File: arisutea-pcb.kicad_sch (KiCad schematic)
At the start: 41 parts, among them U1 USBLC6-2SC6, U2 ATMEGA32U4_QFN44, Y1 16MHz_Crystal_GND24

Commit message: added MOAR LEDZZZZZZZZZ
5 more to be exact.
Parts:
- LOGO3, LOGO4: value QMK Logo -> mattyams logo; footprint arisutea:OSHW-Logo_11.4x12mm_SilkScreen -> 3x6_graphics:mattyams_logo

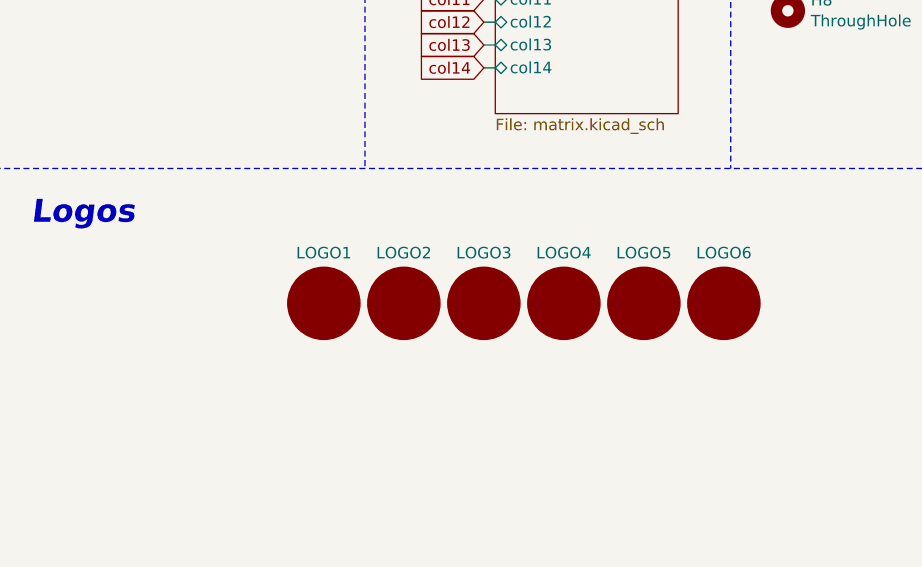
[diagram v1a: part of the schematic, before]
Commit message: added different logo, redid gerbies
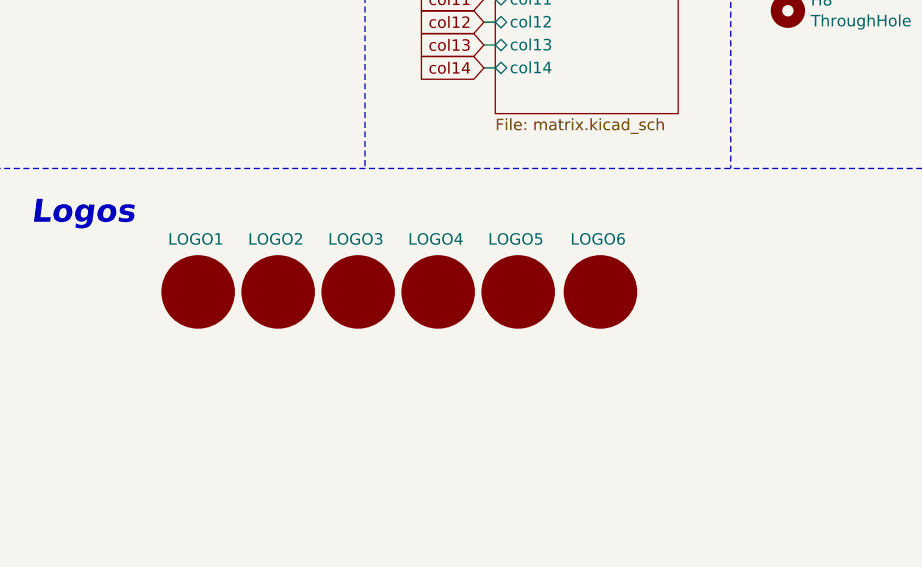
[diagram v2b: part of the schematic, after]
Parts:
- LOGO3, LOGO4: value mattyams logo -> OSHW Logo; footprint 3x6_graphics:mattyams_logo -> arisutea:OSHW-Logo_11.4x12mm_SilkScreen
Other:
- moved on the sheet: LOGO1, LOGO2, LOGO3, LOGO4, LOGO5, LOGO6
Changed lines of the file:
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@@
     (pin "C")
   )
-  (symbol (lib_id "arisutea-pcb:LOGO") (at 213.614 158.242 0) (unit 1)
-    (in_bom yes) (on_board yes)
-    (property "Reference" "LOGO1" (id 0) (at 213.614 152.654 0))
-    (property "Value" "arisutea_logo" (id 1) (at 215.519 148.7424 0)
-      (effects (font (size 1.27 1.27)) hide)
-    )
-    (property "Footprint" "arisutea:arisutea_logo" (id 2) (at 213.614 149.352 0)
-      (effects (font (size 1.27 1.27)) hide)
-    )
-    (property "Datasheet" "" (id 3) (at 213.614 149.352 0)
-      (effects (font (size 1.27 1.27)) hide)
-    )
-  )
-  (symbol (lib_id "arisutea-pcb:LOGO") (at 222.504 158.242 0) (unit 1)
-    (in_bom yes) (on_board yes)
-    (property "Reference" "LOGO2" (id 0) (at 222.504 152.654 0))
-    (property "Value" "arisutea_logo" (id 1) (at 224.409 148.7424 0)
-      (effects (font (size 1.27 1.27)) hide)
-    )
-    (property "Footprint" "arisutea:arisutea_logo" (id 2) (at 222.504 149.352 0)
-      (effects (font (size 1.27 1.27)) hide)
-    )
-    (property "Datasheet" "" (id 3) (at 222.504 149.352 0)
-      (effects (font (size 1.27 1.27)) hide)
-    )
-  )
-  (symbol (lib_id "arisutea-pcb:LOGO") (at 231.394 158.242 0) (unit 1)
-    (in_bom yes) (on_board yes)
-    (property "Reference" "LOGO3" (id 0) (at 231.394 152.654 0))
-    (property "Value" "mattyams logo" (id 1) (at 233.299 148.7424 0)
-      (effects (font (size 1.27 1.27)) hide)
-    )
-    (property "Footprint" "3x6_graphics:mattyams_logo" (id 2) (at 231.394 149.352 0)
-      (effects (font (size 1.27 1.27)) hide)
-    )
-    (property "Datasheet" "" (id 3) (at 231.394 149.352 0)
-      (effects (font (size 1.27 1.27)) hide)
-    )
-  )
-  (symbol (lib_id "arisutea-pcb:LOGO") (at 240.284 158.242 0) (unit 1)
-    (in_bom yes) (on_board yes)
-    (property "Reference" "LOGO4" (id 0) (at 240.284 152.654 0))
-    (property "Value" "mattyams logo" (id 1) (at 242.189 148.7424 0)
-      (effects (font (size 1.27 1.27)) hide)
-    )
-    (property "Footprint" "3x6_graphics:mattyams_logo" (id 2) (at 240.284 149.352 0)
-      (effects (font (size 1.27 1.27)) hide)
-    )
-    (property "Datasheet" "" (id 3) (at 240.284 149.352 0)
-      (effects (font (size 1.27 1.27)) hide)
-    )
-  )
-  (symbol (lib_id "arisutea-pcb:LOGO") (at 249.174 158.242 0) (unit 1)
-    (in_bom yes) (on_board yes)
-    (property "Reference" "LOGO5" (id 0) (at 249.174 152.654 0))
-    (property "Value" "QMK_Logo_Light" (id 1) (at 251.079 148.7424 0)
-      (effects (font (size 1.27 1.27)) hide)
-    )
-    (property "Footprint" "arisutea:QMK_Logo_Light" (id 2) (at 249.174 149.352 0)
-      (effects (font (size 1.27 1.27)) hide)
-    )
-    (property "Datasheet" "" (id 3) (at 249.174 149.352 0)
-      (effects (font (size 1.27 1.27)) hide)
-    )
-  )
-  (symbol (lib_id "arisutea-pcb:LOGO") (at 258.064 158.242 0) (unit 1)
-    (in_bom yes) (on_board yes)
-    (property "Reference" "LOGO6" (id 0) (at 258.064 152.654 0))
-    (property "Value" "QMK_Logo_Light" (id 1) (at 259.969 148.7424 0)
-      (effects (font (size 1.27 1.27)) hide)
-    )
-    (property "Footprint" "arisutea:QMK_Logo_Light" (id 2) (at 258.064 149.352 0)
-      (effects (font (size 1.27 1.27)) hide)
-    )
-    (property "Datasheet" "" (id 3) (at 258.064 149.352 0)
+  (symbol (lib_id "arisutea-pcb:LOGO") (at 199.644 156.972 0) (unit 1)
+    (in_bom yes) (on_board yes)
+    (property "Reference" "LOGO1" (id 0) (at 199.39 151.13 0))
+    (property "Value" "arisutea_logo" (id 1) (at 201.549 147.4724 0)
+      (effects (font (size 1.27 1.27)) hide)
+    )
+    (property "Footprint" "arisutea:arisutea_logo" (id 2) (at 199.644 148.082 0)
+      (effects (font (size 1.27 1.27)) hide)
+    )
+    (property "Datasheet" "" (id 3) (at 199.644 148.082 0)
+      (effects (font (size 1.27 1.27)) hide)
+    )
+  )
+  (symbol (lib_id "arisutea-pcb:LOGO") (at 208.534 156.972 0) (unit 1)
+    (in_bom yes) (on_board yes)
+    (property "Reference" "LOGO2" (id 0) (at 208.28 151.13 0))
+    (property "Value" "arisutea_logo" (id 1) (at 210.439 147.4724 0)
+      (effects (font (size 1.27 1.27)) hide)
+    )
+    (property "Footprint" "arisutea:arisutea_logo" (id 2) (at 208.534 148.082 0)
+      (effects (font (size 1.27 1.27)) hide)
+    )
+    (property "Datasheet" "" (id 3) (at 208.534 148.082 0)
+      (effects (font (size 1.27 1.27)) hide)
+    )
+  )
+  (symbol (lib_id "arisutea-pcb:LOGO") (at 217.424 156.972 0) (unit 1)
+    (in_bom yes) (on_board yes)
+    (property "Reference" "LOGO3" (id 0) (at 217.17 151.13 0))
+    (property "Value" "OSHW Logo" (id 1) (at 219.329 147.4724 0)
+      (effects (font (size 1.27 1.27)) hide)
+    )
+    (property "Footprint" "arisutea:OSHW-Logo_11.4x12mm_SilkScreen" (id 2) (at 217.424 148.082 0)
+      (effects (font (size 1.27 1.27)) hide)
+    )
+    (property "Datasheet" "" (id 3) (at 217.424 148.082 0)
+      (effects (font (size 1.27 1.27)) hide)
+    )
+  )
+  (symbol (lib_id "arisutea-pcb:LOGO") (at 226.314 156.972 0) (unit 1)
+    (in_bom yes) (on_board yes)
+    (property "Reference" "LOGO4" (id 0) (at 226.06 151.13 0))
+    (property "Value" "OSHW Logo" (id 1) (at 228.219 147.4724 0)
+      (effects (font (size 1.27 1.27)) hide)
+    )
+    (property "Footprint" "arisutea:OSHW-Logo_11.4x12mm_SilkScreen" (id 2) (at 226.314 148.082 0)
+      (effects (font (size 1.27 1.27)) hide)
+    )
+    (property "Datasheet" "" (id 3) (at 226.314 148.082 0)
+      (effects (font (size 1.27 1.27)) hide)
+    )
+  )
+  (symbol (lib_id "arisutea-pcb:LOGO") (at 235.204 156.972 0) (unit 1)
+    (in_bom yes) (on_board yes)
+    (property "Reference" "LOGO5" (id 0) (at 234.95 151.13 0))
+    (property "Value" "QMK_Logo_Light" (id 1) (at 237.109 147.4724 0)
+      (effects (font (size 1.27 1.27)) hide)
+    )
+    (property "Footprint" "arisutea:QMK_Logo_Light" (id 2) (at 235.204 148.082 0)
+      (effects (font (size 1.27 1.27)) hide)
+    )
+    (property "Datasheet" "" (id 3) (at 235.204 148.082 0)
+      (effects (font (size 1.27 1.27)) hide)
+    )
+  )
+  (symbol (lib_id "arisutea-pcb:LOGO") (at 244.348 156.972 0) (unit 1)
+    (in_bom yes) (on_board yes)
+    (property "Reference" "LOGO6" (id 0) (at 244.094 151.13 0))
+    (property "Value" "QMK_Logo_Light" (id 1) (at 246.253 147.4724 0)
+      (effects (font (size 1.27 1.27)) hide)
+    )
+    (property "Footprint" "arisutea:QMK_Logo_Light" (id 2) (at 244.348 148.082 0)
+      (effects (font (size 1.27 1.27)) hide)
+    )
+    (property "Datasheet" "" (id 3) (at 244.348 148.082 0)
       (effects (font (size 1.27 1.27)) hide)
     )
@@
     )
     (path "/00000000-0000-0000-0000-00006062f214"
-      (reference "LOGO3") (unit 1) (value "mattyams logo") (footprint "3x6_graphics:mattyams_logo")
+      (reference "LOGO3") (unit 1) (value "OSHW Logo") (footprint "arisutea:OSHW-Logo_11.4x12mm_SilkScreen")
     )
     (path "/00000000-0000-0000-0000-00006062f624"
-      (reference "LOGO4") (unit 1) (value "mattyams logo") (footprint "3x6_graphics:mattyams_logo")
+      (reference "LOGO4") (unit 1) (value "OSHW Logo") (footprint "arisutea:OSHW-Logo_11.4x12mm_SilkScreen")
     )
     (path "/00000000-0000-0000-0000-00006063ab78"

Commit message: Rev 0.4
Added more LEDs, moved some traces around, updated iBOM, added new renders...and things
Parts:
- C4: value 1uF (±10%) -> 1uF
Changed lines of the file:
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@@
   (symbol (lib_id "arisutea-pcb:Device_C_Small") (at 98.552 88.138 0) (unit 1)
     (in_bom yes) (on_board yes)
-    (property "Reference" "C4" (id 0) (at 95.3262 90.17 0)
-      (effects (font (size 1.27 1.27)) (justify left))
-    )
-    (property "Value" "1uF (±10%)" (id 1) (at 100.9396 93.2434 90)
+    (property "Reference" "C4" (id 0) (at 93.5482 87.122 0)
+      (effects (font (size 1.27 1.27)) (justify left))
+    )
+    (property "Value" "1uF" (id 1) (at 93.0656 88.9254 0)
       (effects (font (size 1.27 1.27)) (justify left))
     )
@@
     )
     (path "/00000000-0000-0000-0000-00005c4b33f7"
-      (reference "C4") (unit 1) (value "1uF (±10%)") (footprint "arisutea:C_0805_2012Metric_Pad1.18x1.45mm_HandSolder")
+      (reference "C4") (unit 1) (value "1uF") (footprint "arisutea:C_0805_2012Metric_Pad1.18x1.45mm_HandSolder")
     )
     (path "/00000000-0000-0000-0000-00005c4d647d"

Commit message: add pretty logo
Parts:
- LOGO1, LOGO2: footprint arisutea:arisutea_logo -> arisutea:arisutea_logo_copper
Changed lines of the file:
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@@
   (title_block
     (title "Arisutea RGB Keyboard")
-    (date "2021-06-19")
-    (rev "0.3")
+    (date "2021-12-20")
+    (rev "0.4w")
     (company "mattyams")
   )
@@
       (effects (font (size 1.27 1.27)) hide)
     )
-    (property "Footprint" "arisutea:arisutea_logo" (id 2) (at 199.644 148.082 0)
+    (property "Footprint" "arisutea:arisutea_logo_copper" (id 2) (at 199.644 148.082 0)
       (effects (font (size 1.27 1.27)) hide)
     )
@@
       (effects (font (size 1.27 1.27)) hide)
     )
-    (property "Footprint" "arisutea:arisutea_logo" (id 2) (at 208.534 148.082 0)
+    (property "Footprint" "arisutea:arisutea_logo_copper" (id 2) (at 208.534 148.082 0)
       (effects (font (size 1.27 1.27)) hide)
     )
@@
     )
     (path "/00000000-0000-0000-0000-00006042e29e"
-      (reference "LOGO1") (unit 1) (value "arisutea_logo") (footprint "arisutea:arisutea_logo")
+      (reference "LOGO1") (unit 1) (value "arisutea_logo") (footprint "arisutea:arisutea_logo_copper")
     )
     (path "/00000000-0000-0000-0000-0000605b7585"
-      (reference "LOGO2") (unit 1) (value "arisutea_logo") (footprint "arisutea:arisutea_logo")
+      (reference "LOGO2") (unit 1) (value "arisutea_logo") (footprint "arisutea:arisutea_logo_copper")
     )
     (path "/00000000-0000-0000-0000-00006062f214"
